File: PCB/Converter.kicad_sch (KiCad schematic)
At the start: 84 parts, among them Q1 ${MFGPN}, Q12 HUASHUO HSBB0115, Q2 ${MFGPN}, Q3 ${MFGPN}, Q4 ${MFGPN}, Q5 HUASHUO HSBB0115, U1 LT8390AIUFD-PBF

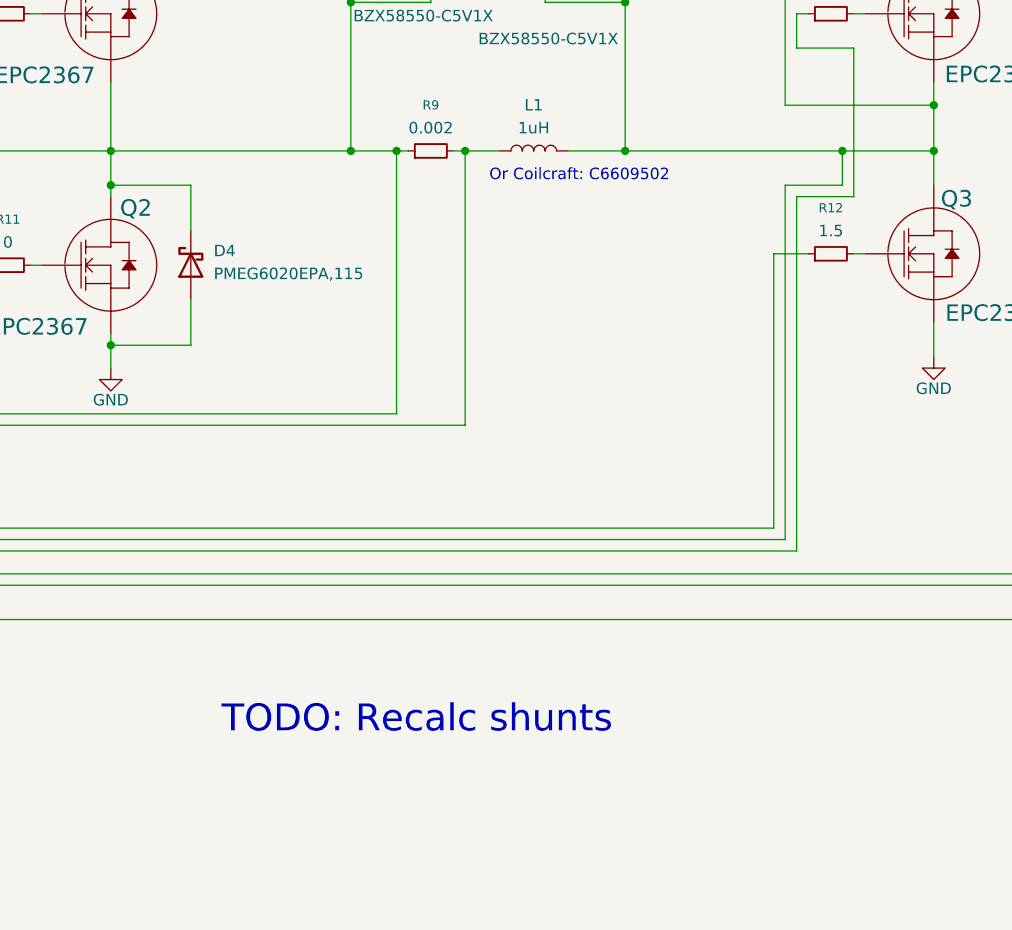
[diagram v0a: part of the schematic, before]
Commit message: Implemented partial refresh
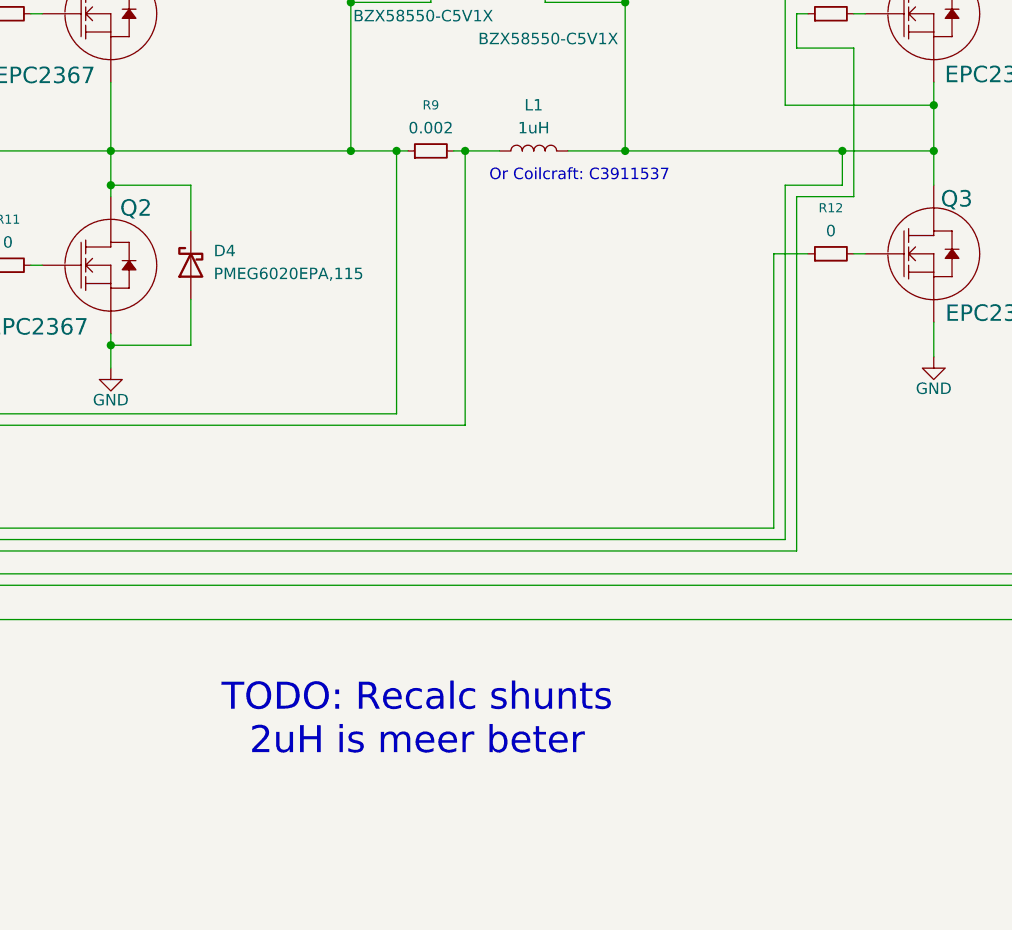
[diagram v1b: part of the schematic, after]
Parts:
- R12: value 1.5 -> 0
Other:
- note added: "Or Coilcraft: C3911537"
- note added: "TODO: Recalc shunts 2uH is meer beter"
- note removed: "Or Coilcraft: C6609502"
- note removed: "TODO: Recalc shunts"
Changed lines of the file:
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@@
 		(rev "R1")
 	)
-	(text "Or Coilcraft: C6609502"
+	(text "Or Coilcraft: C3911537"
 		(exclude_from_sim no)
 		(at 254 147.574 0)
@@
 		)
 	)
-	(text "TODO: Recalc shunts"
+	(text "TODO: Recalc shunts\n2uH is meer beter\n"
 		(exclude_from_sim no)
 		(at 235.966 208.026 0)
@@
 			)
 		)
-		(property "Value" "1.5"
+		(property "Value" "0"
 			(at 281.94 153.67 90)
 			(show_name no)

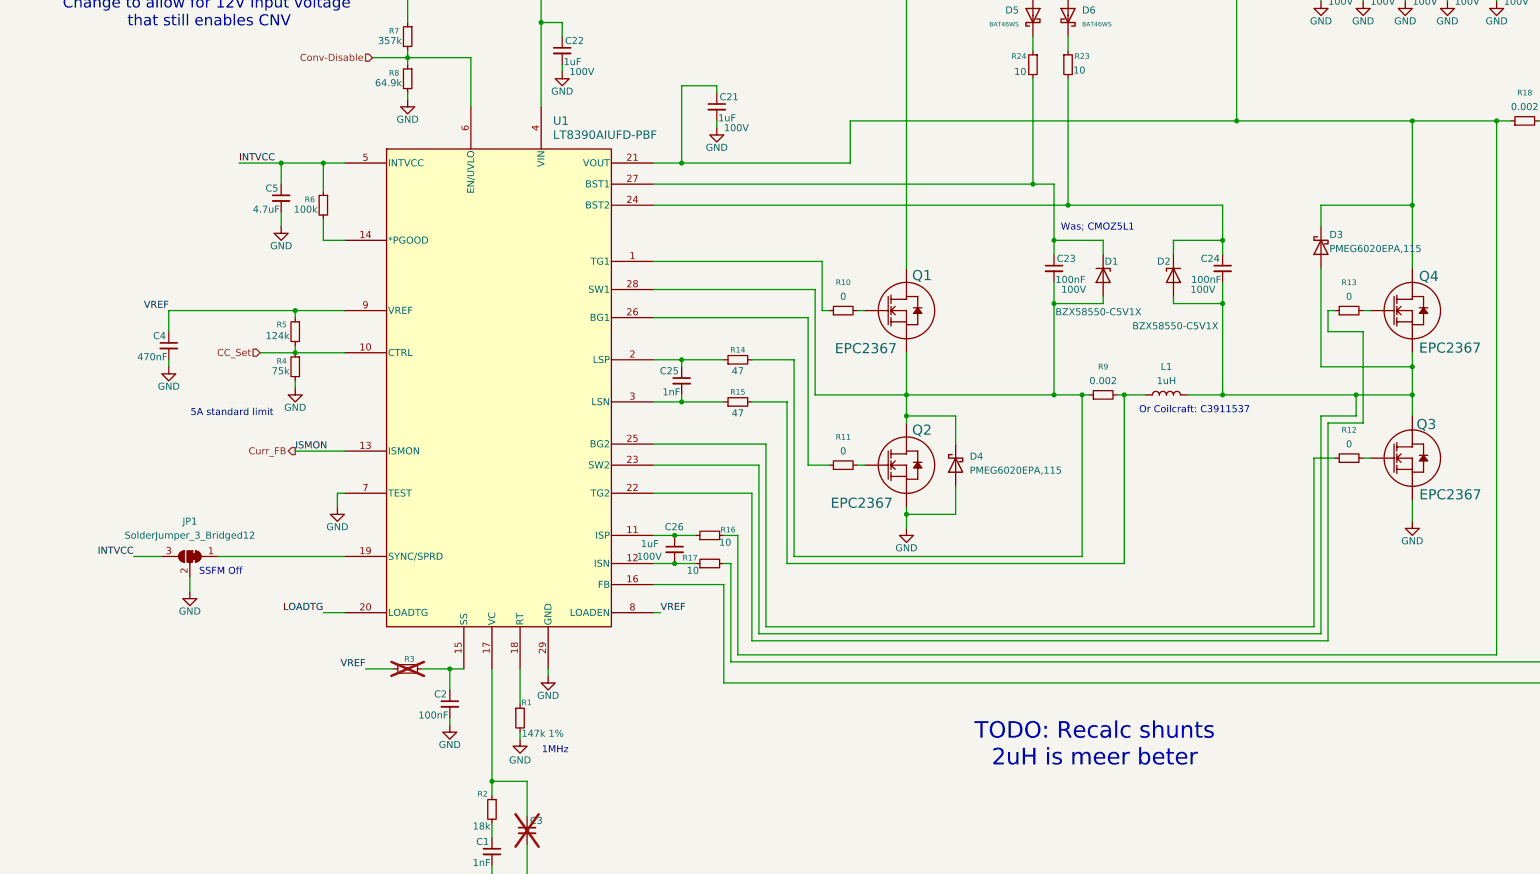
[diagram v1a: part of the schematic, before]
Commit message: Revision 2; gate diodes, 5V into LT, i2c and uart lines fixed
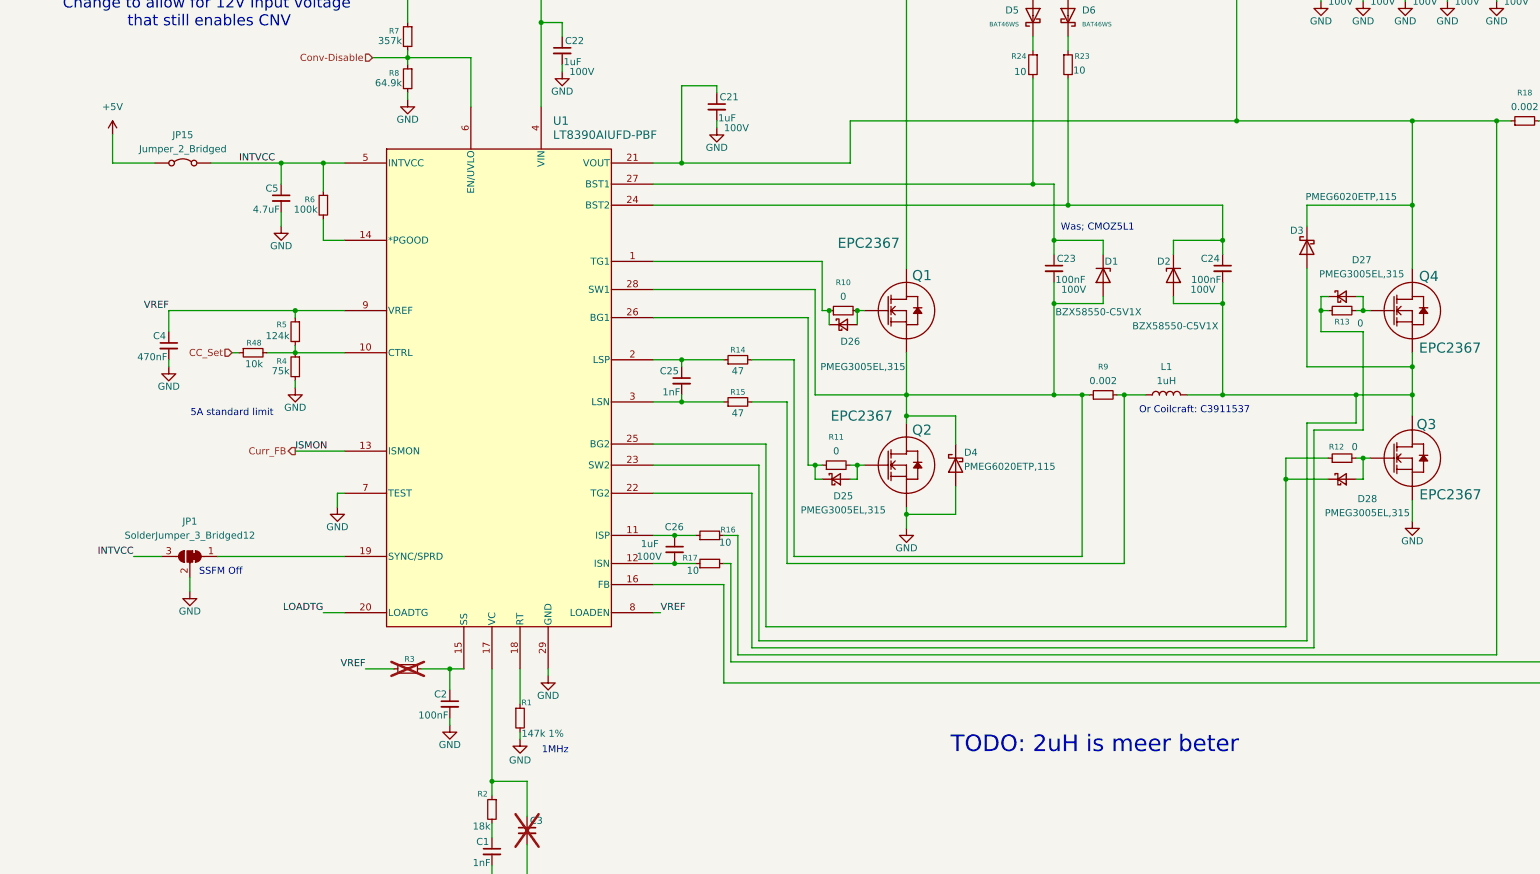
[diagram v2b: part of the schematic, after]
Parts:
- removed D4: PMEG6020EPA,115, thommys-parts2:DFN2020-3_L2.0-W2.0-P0.65-BR-1, symbol Thommys-parts2:D_Schottky_3
- added D25, D26, D27, D28: PMEG3005EL,315, Diode_SMD:D_SOD-882, symbol Device:D_Schottky_Small
- added D4: PMEG6020ETP,115, Diode_SMD:D_SOD-128, symbol Device:D_Schottky
- added JP15: Jumper_2_Bridged, Jumper:SolderJumper-2_P1.3mm_Open_RoundedPad1.0x1.5mm, symbol Jumper:Jumper_2_Bridged
- added R48: 10k, Resistor_SMD:R_0402_1005Metric, symbol Device:R_Small
- D3: value PMEG6020EPA,115 -> PMEG6020ETP,115; footprint thommys-parts2:DFN2020-3_L2.0-W2.0-P0.65-BR-1 -> Diode_SMD:D_SOD-128; symbol Thommys-parts2:D_Schottky_3 -> Device:D_Schottky; LCSC C42237120 -> C179434
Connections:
- net CC_Set: now also R48.1; no longer R4.1, R5.2, U1.10 (CTRL)
- net GND: now also D4.2 (A)
- net INTVCC: now also JP15.2 (B)
- net at Q3.1 (G), R12.2: now also D28.2 (A)
- net at C24.2, D2.2 (A), L1.2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: now also D3.2 (A); no longer D3.A
- net at C16.1, C17.1, C18.1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: now also D3.1 (K); no longer D3.K
- net at C23.2, D1.2 (A), Q1.2 (S)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: now also D4.1 (K)
- net at R12.1, U1.25 (BG2): now also D28.1 (K)
- net at R10.1, U1.1 (TG1): now also D26.1 (K)
- net at R13.1, U1.22 (TG2): now also D27.1 (K)
- net at R11.1, U1.26 (BG1): now also D25.1 (K)
- net at Q1.1 (G), R10.2: now also D26.2 (A)
- net at Q2.1 (G), R11.2: now also D25.2 (A)
- net at Q4.1 (G), R13.2: now also D27.2 (A)
- new net: R4.1, R48.2, R5.2, U1.10 (CTRL)
- new net +5V: JP15.1 (A)
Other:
- note added: "TODO: 2uH is meer beter"
- note removed: "TODO: Recalc shunts 2uH is meer beter"
- moved on the sheet: D3, R11, R12, R13

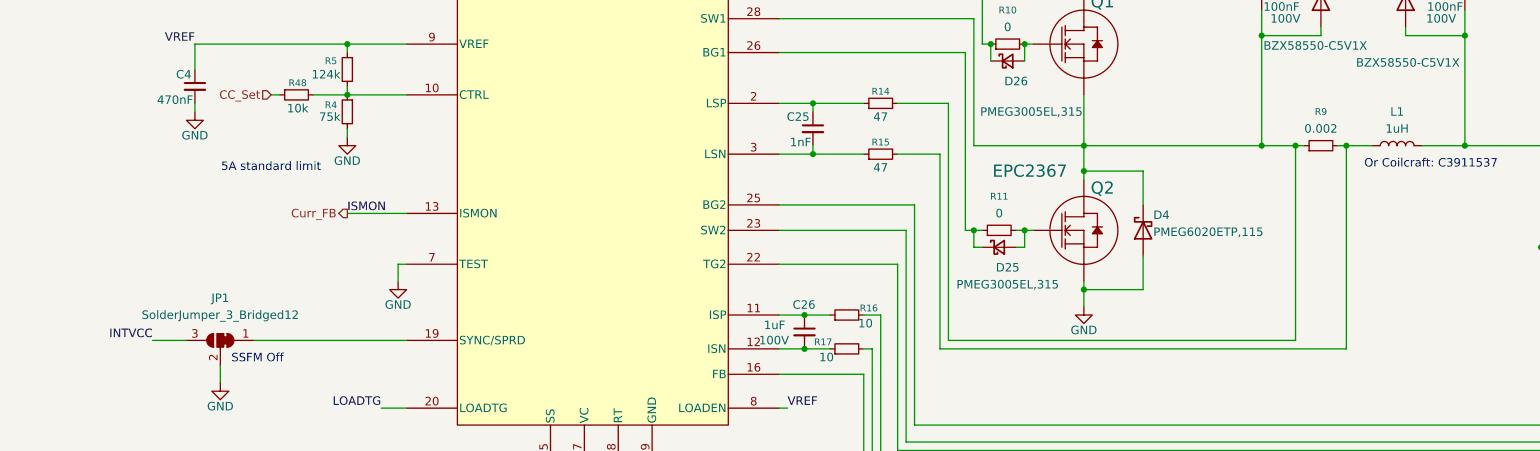
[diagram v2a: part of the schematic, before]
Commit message: Changed inductor to much better one
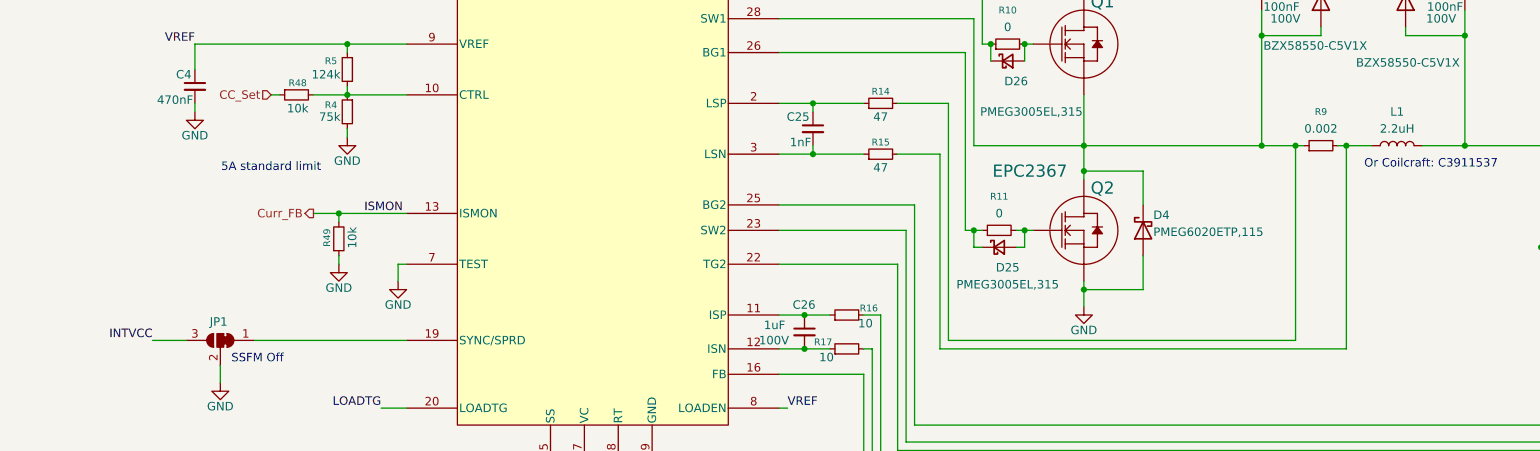
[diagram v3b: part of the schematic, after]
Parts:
- added R49: 10k, Resistor_SMD:R_0402_1005Metric, symbol Device:R_Small
- L1: value 1uH -> 2.2uH; footprint thommys-parts2:IND-SMD_SL1265-101M -> thommys-parts2:IND-SMD_L7.5-W7.2-1; JLC C22463848 -> C5125746; LCSC C22463848 -> C5125746
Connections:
- net Curr_FB: now also R49.2
- net GND: now also R49.1
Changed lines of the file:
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@@
 	)
 	(junction
+		(at 90.17 154.94)
+		(diameter 0)
+		(color 0 0 0 0)
+	)
+	(junction
 		(at 388.62 95.25)
 		(diameter 0)
@@
 	(wire
 		(pts
+			(xy 90.17 161.29) (xy 90.17 162.56)
+		)
+		(stroke
+			(width 0)
+			(type default)
+		)
+	)
+	(wire
+		(pts
 			(xy 119.38 203.2) (xy 119.38 204.47)
 		)
@@
 	(wire
 		(pts
+			(xy 90.17 156.21) (xy 90.17 154.94)
+		)
+		(stroke
+			(width 0)
+			(type default)
+		)
+	)
+	(wire
+		(pts
 			(xy 186.69 129.54) (xy 186.69 120.65)
 		)
@@
 	(wire
 		(pts
+			(xy 90.17 154.94) (xy 100.33 154.94)
+		)
+		(stroke
+			(width 0)
+			(type default)
+		)
+	)
+	(wire
+		(pts
 			(xy 328.93 95.25) (xy 335.28 95.25)
 		)
@@
 	(wire
 		(pts
-			(xy 91.44 154.94) (xy 100.33 154.94)
+			(xy 86.36 154.94) (xy 90.17 154.94)
 		)
 		(stroke
@@
 	)
 	(label "ISMON"
-		(at 91.44 154.94 0)
+		(at 93.98 154.94 0)
 		(effects
 			(font
@@
 	(hierarchical_label "Curr_FB"
 		(shape output)
-		(at 91.44 154.94 180)
+		(at 86.36 154.94 180)
 		(effects
 			(font
@@
 	)
 	(symbol
+		(lib_id "power:GND")
+		(at 90.17 162.56 0)
+		(unit 1)
+		(body_style 1)
+		(exclude_from_sim no)
+		(in_bom yes)
+		(on_board yes)
+		(in_pos_files yes)
+		(dnp no)
+		(property "Reference" "#PWR068"
+			(at 90.17 168.91 0)
+			(hide yes)
+			(show_name no)
+			(do_not_autoplace no)
+			(effects
+				(font
+					(size 1.27 1.27)
+				)
+			)
+		)
+		(property "Value" "GND"
+			(at 90.17 166.116 0)
+			(show_name no)
+			(do_not_autoplace no)
+			(effects
+				(font
+					(size 1.27 1.27)
+				)
+			)
+		)
+		(property "Footprint" ""
+			(at 90.17 162.56 0)
+			(hide yes)
+			(show_name no)
+			(do_not_autoplace no)
+			(effects
+				(font
+					(size 1.27 1.27)
+				)
+			)
+		)
+		(property "Datasheet" ""
+			(at 90.17 162.56 0)
+			(hide yes)
+			(show_name no)
+			(do_not_autoplace no)
+			(effects
+				(font
+					(size 1.27 1.27)
+				)
+			)
+		)
+		(property "Description" "Power symbol creates a global label with name \"GND\" , ground"
+			(at 90.17 162.56 0)
+			(hide yes)
+			(show_name no)
+			(do_not_autoplace no)
+			(effects
+				(font
+					(size 1.27 1.27)
+				)
+			)
+		)
+		(pin "1"
+		)
+		(instances
+			(project "nitride-nano"
+				(path "/aaad0350-e7db-44d5-b7ef-99e6416f6948/f0962043-1aad-4f17-a8f7-b50910365543"
+					(reference "#PWR068")
+					(unit 1)
+				)
+			)
+		)
+	)
+	(symbol
 		(lib_id "Device:R_Small")
 		(at 325.12 200.66 0)
@@
 		(dnp no)
 		(property "Reference" "JP1"
-			(at 72.39 167.64 0)
+			(at 72.136 171.196 0)
 			(show_name no)
 			(do_not_autoplace no)
@@
 		(property "Value" "SolderJumper_3_Bridged12"
 			(at 72.39 170.18 0)
+			(hide yes)
 			(show_name no)
 			(do_not_autoplace no)
@@
 	(symbol
 		(lib_id "Device:R_Small")
+		(at 90.17 158.75 0)
+		(mirror x)
+		(unit 1)
+		(body_style 1)
+		(exclude_from_sim no)
+		(in_bom yes)
+		(on_board yes)
+		(in_pos_files yes)
+		(dnp no)
+		(property "Reference" "R49"
+			(at 88.392 157.2105 90)
+			(show_name no)
+			(do_not_autoplace no)
+			(effects
+				(font
+					(size 1.016 1.016)
+				)
+				(justify left)
+			)
+		)
+		(property "Value" "10k"
+			(at 92.202 156.9565 90)
+			(show_name no)
+			(do_not_autoplace no)
+			(effects
+				(font
+					(size 1.27 1.27)
+				)
+				(justify left)
+			)
+		)
+		(property "Footprint" "Resistor_SMD:R_0402_1005Metric"
+			(at 90.17 158.75 0)
+			(hide yes)
+			(show_name no)
+			(do_not_autoplace no)
+			(effects
+				(font
+					(size 1.27 1.27)
+				)
+			)
+		)
+		(property "Datasheet" ""
+			(at 90.17 158.75 0)
+			(hide yes)
+			(show_name no)
+			(do_not_autoplace no)
+			(effects
+				(font
+					(size 1.27 1.27)
+				)
+			)
+		)
+		(property "Description" "Resistor, small symbol"
+			(at 90.17 158.75 0)
+			(hide yes)
+			(show_name no)
+			(do_not_autoplace no)
+			(effects
+				(font
+					(size 1.27 1.27)
+				)
+			)
+		)
+		(property "LCSC" "C2906861"
+			(at 91.694 159.766 0)
+			(hide yes)
+			(show_name no)
+			(do_not_autoplace no)
+			(effects
+				(font
+					(size 1.27 1.27)
+				)
+			)
+		)
+		(pin "1"
+		)
+		(pin "2"
+		)
+		(instances
+			(project "nitride-nano"
+				(path "/aaad0350-e7db-44d5-b7ef-99e6416f6948/f0962043-1aad-4f17-a8f7-b50910365543"
+					(reference "R49")
+					(unit 1)
+				)
+			)
+		)
+	)
+	(symbol
+		(lib_id "Device:R_Small")
 		(at 360.68 77.47 180)
 		(unit 1)
@@
 			)
 		)
-		(property "Value" "1uH"
+		(property "Value" "2.2uH"
 			(at 248.92 142.24 90)
 			(show_name no)
@@
 			)
 		)
-		(property "Footprint" "thommys-parts2:IND-SMD_SL1265-101M"
+		(property "Footprint" "thommys-parts2:IND-SMD_L7.5-W7.2-1"
 			(at 248.92 144.78 0)
 			(hide yes)
@@
 			)
 		)
-		(property "JLC" "C22463848"
+		(property "JLC" "C5125746"
 			(at 248.92 144.78 90)
 			(hide yes)
@@
 			)
 		)
-		(property "LCSC" "C22463848"
+		(property "LCSC" "C5125746"
 			(at 248.92 139.7 0)
 			(hide yes)
